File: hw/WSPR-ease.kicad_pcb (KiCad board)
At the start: 4 copper layers, 99 x 64 mm, 168 parts, among them IC401 SN74AHCT1G125DRLR, IC402 SN74AHCT1G125DRLR, IC403 SN74AHCT1G125DRLR, IC501 SN74AHCT1G125DRLR, IC502 SN74AHCT1G125DRLR, IC503 SN74AHCT1G125DRLR, IC601 SN74AHCT1G125DRLR, IC602 SN74AHCT1G125DRLR, IC603 SN74AHCT1G125DRLR, IC701 SN74AHCT1G125DRLR, IC702 SN74AHCT1G125DRLR, IC703 SN74AHCT1G125DRLR, J101 SMA, J102 pwr+data, J103 SMA, Q101 MMBF170, Q401 MMBF170, Q402 MMBF170, Q403 MMBF170, Q501 MMBF170, Q502 MMBF170, Q503 MMBF170, Q601 MMBF170, Q602 MMBF170, Q603 MMBF170, Q701 MMBF170, Q702 MMBF170, Q703 MMBF170, T301 BN-43-202_DualPri_CTSec, U101 GNSS module, U102 ESP32-S3-WROOM-1-N8R8, U103 SRV05-4, U104 TPS74612PQWDRBRQ1, U105 TPS22918DBVR, U106 LMR51430YDDCR, U201 AS183-92LF, U202 AS183-92LF, U203 AS183-92LF, U204 AS183-92LF, U301 ICE40UP5K-SG48ITR, Y301 40MHz

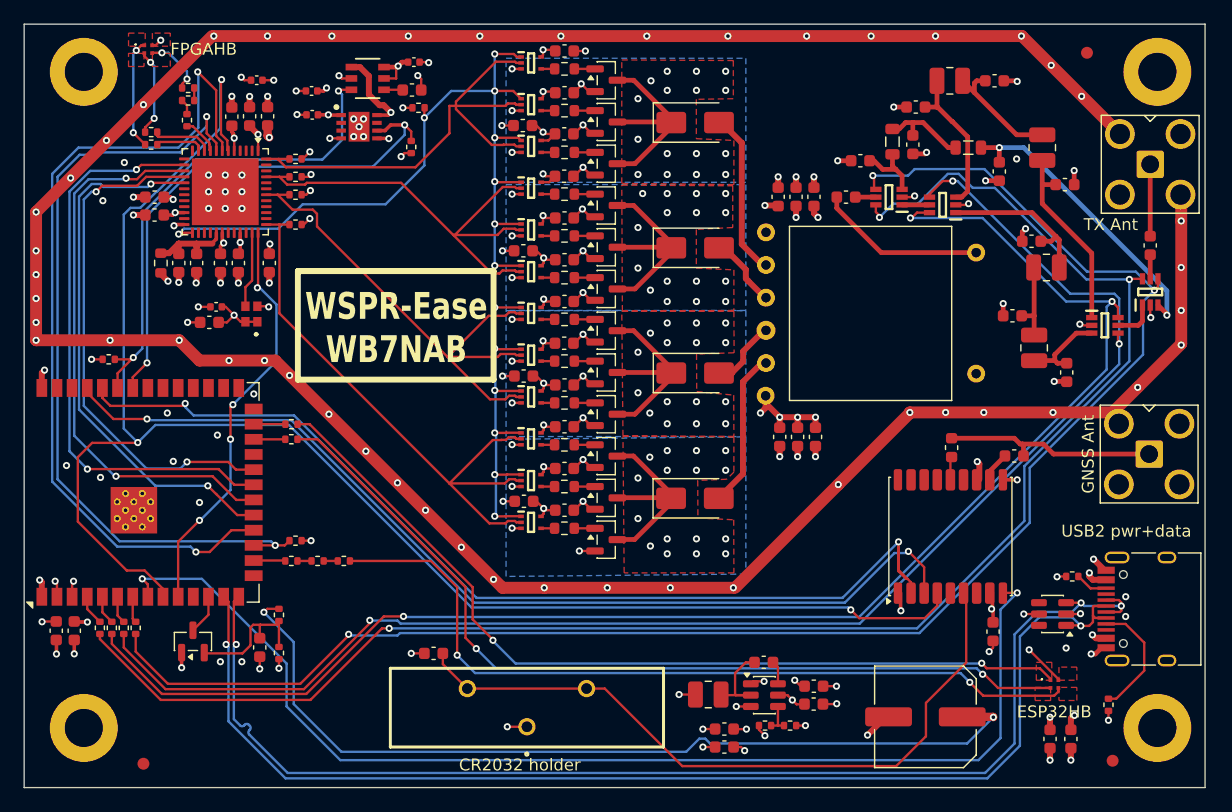
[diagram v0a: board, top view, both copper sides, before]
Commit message: Use relays and do layout over again to make these damned things fit
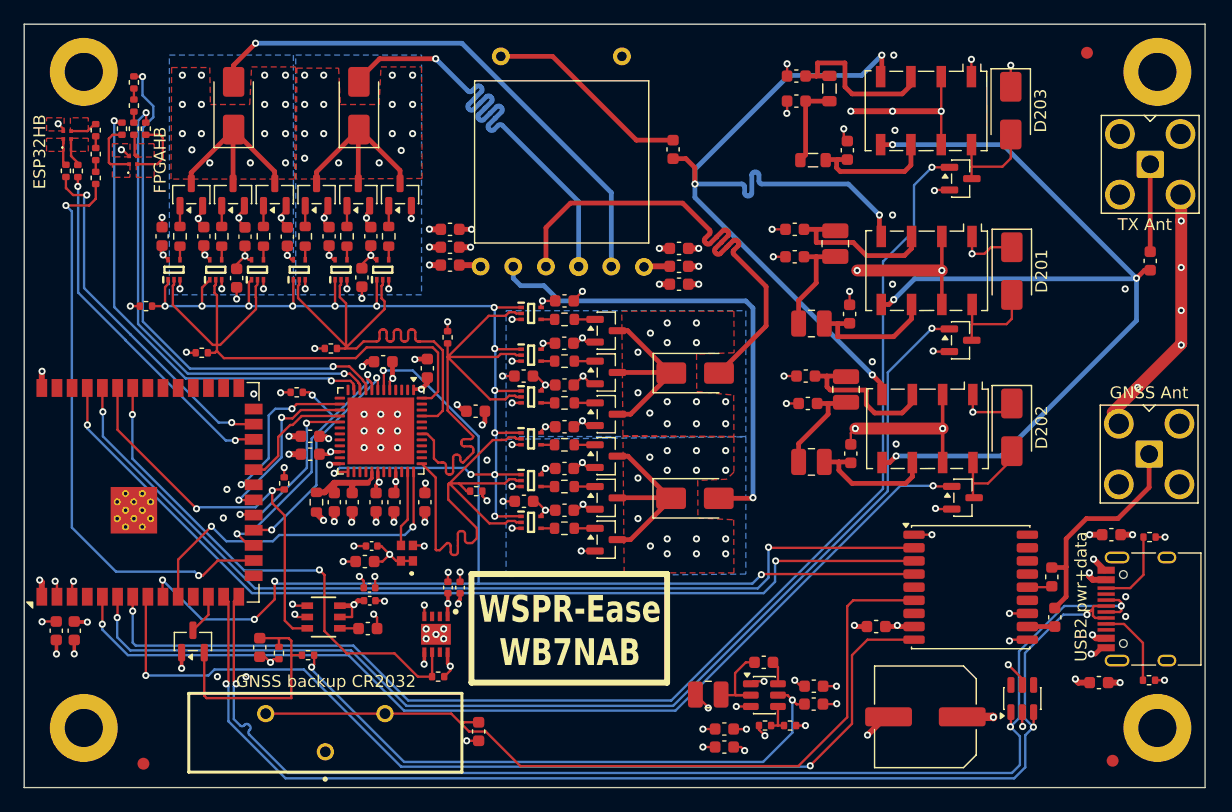
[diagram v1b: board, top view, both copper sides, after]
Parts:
- removed R103, R104, R105, R106: 22, Resistor_SMD:R_0402_1005Metric
- removed U201, U202, U203, U204: AS183-92LF, Library:SOT65P220X110-6N
- added D201: SS14, Diode_SMD:D_SMA, F.Cu at (132.4, 90.1)
- added D202: SS14, Diode_SMD:D_SMA, F.Cu at (132.4, 103.2)
- added D203: SS14, Diode_SMD:D_SMA, F.Cu at (132.3, 76.7)
- added K201: G6K-2, Relay_SMD:Relay_DPDT_Omron_G6K-2G, F.Cu at (125.3, 103.3)
- added K202: G6K-2, Relay_SMD:Relay_DPDT_Omron_G6K-2G, F.Cu at (125.3, 90.0)
- added K203: G6K-2, Relay_SMD:Relay_DPDT_Omron_G6K-2G, F.Cu at (125.2, 76.7)
- added Q201: 2N7002H, Package_TO_SOT_SMD:SOT-23, F.Cu at (128.3, 109.1)
- added Q202: 2N7002H, Package_TO_SOT_SMD:SOT-23, F.Cu at (128.1, 95.9)
- added Q203: 2N7002H, Package_TO_SOT_SMD:SOT-23, F.Cu at (128.1, 82.3)
- BT101: value CR2032 holder -> CR3032 holder
- Q101: value MMBF170 -> 2N7002H
- moved D101 94.7 mm to (53.2, 78.7), turned to 90 degrees
- moved C109 45.3 mm to (78.6, 117.7)
- moved C107 45.3 mm to (78.4, 120.1)
- moved U105 45.3 mm to (74.7, 119.1)
- moved R108 44.5 mm to (84.3, 124.1), turned to 0 degrees
- moved C320 43.6 mm to (78.5, 116.7), turned to 0 degrees
- moved C324 43.4 mm to (86.1, 116.6), turned to 90 degrees
- moved U104 43.0 mm to (84.1, 120.5), turned to -90 degrees
- moved R113 41.7 mm to (55.6, 78.3), turned to 90 degrees
- moved C108 41.2 mm to (85.1, 116.6), turned to 90 degrees
- moved R110 38.9 mm to (55.6, 80.3), turned to 90 degrees
- moved D701 38.7 mm to (67.2, 76.2), turned to 90 degrees
- moved C702 37.1 mm to (61.2, 87.2), turned to -90 degrees
- moved Q701 36.1 mm to (63.6, 83.7), turned to 90 degrees
- moved R107 36.1 mm to (55.6, 82.3), turned to 90 degrees
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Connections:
- T301 pad 2: /Transmitter/push2T -> /Transmitter/pull2T
- T301 pad 3: /Transmitter/push1T -> /Transmitter/pull1T
- T301 pad 4: /Transmitter/pull1T -> /Transmitter/push1T
- T301 pad 5: /Transmitter/pull2T -> /Transmitter/push2T
- U102 pad 4: Net-(U102-IO4) -> unconnected-(U102-IO4-Pad4)
- U102 pad 5: Net-(U102-IO5) -> /loON
- U102 pad 6: Net-(U102-IO6) -> /midON
- U102 pad 7: Net-(U102-IO7) -> /hiON
- U103 pad 1: /D- -> /D+
- U103 pad 3: /D+ -> /D-
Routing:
- net GND: track 348.6 -> 167.8 mm, vias 177 -> 138
- net /lo1ON: track 126.3 -> 0.00 mm, vias 3 -> 0
- net /lo2ON: track 124.8 -> 0.00 mm, vias 3 -> 0
- net /midON: track 0.00 -> 94.5 mm, vias 0 -> 2
- net Net-(C211-Pad1): track 2.03 -> 79.6 mm, vias 0 -> 4
- net /grn: track 74.1 -> 2.42 mm, vias 2 -> 0
- net /blu: track 73.7 -> 2.26 mm, vias 2 -> 0
- net Net-(C201-Pad2): track 1.72 -> 71.7 mm, vias 0 -> 4
- net /red: track 67.9 -> 2.20 mm, vias 2 -> 0
- net /loON: track 138.6 -> 84.6 mm, vias 3 -> 2
- net /fpgaDONE: track 71.9 -> 18.4 mm
- net Net-(U102-IO46): track 2.61 -> 48.6 mm, vias 0 -> 2
- net /gnssPPS: track 138.0 -> 92.7 mm, vias 3 -> 5
- net /fpgaCRESET: track 67.3 -> 24.8 mm, vias 2 -> 3
- net /Transmitter/hbR: track 3.15 -> 43.5 mm, vias 0 -> 2
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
